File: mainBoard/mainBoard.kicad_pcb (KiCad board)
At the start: 4 copper layers, 221.8 x 118.5 mm, 243 parts, among them J1 1366005, J10 Conn_01x06, J11 Conn_01x07, J12 Conn_01x04, J13 Conn_01x04, J14 1714971, J15 Conn_02x05_Odd_Even, J16 Conn_01x02, J17 Conn_01x05, J18 1714971, J4 4DB-P108-02, J5 4DB-P108-02, J6 4DB-P108-02, J7 Conn_01x02, J8 Conn_01x02, J9 Conn_01x02, K1 Relay_SPDT, Q1 IRLML6244TRPBF, Q2 IRLML6244TRPBF, Q3 IRLML6244TRPBF, Q4 IRLML6244TRPBF, Q5 IRLML6244TRPBF, Q6 IRLML6244TRPBF, Q7 IRLML6244TRPBF, Q8 IRLML6244TRPBF, Q9 IRLML6244TRPBF, SW1 SW_SPST, SW2 SW_SPDT, SW3 SW_Push, SW4 SW_Push, U1 MCP1727T-3302E/SN, U10 DS18B20+, U11 DS18B20+, U12 OPA333AIDCKT, U13 DS18B20+, U14 DS18B20+, U15 DS18B20+, U16 100, U17 100, U18 USBLC6-2SC6, U19 USBLC6-4SC6, U2 AP62250WU, U21 100, U22 USBLC6-4SC6, U23 USBLC6-4SC6, U24 USBLC6-4SC6, U25 USBLC6-4SC6, U3 MCP1727T-3302E/SN, U4 STM32F401RETx, U6 MOC3083S-TA1, U7 MOC3083S-TA1, U8 OPA333AIDCKT, U9 OPA333AIDCKT, Y1 ATS240C-E

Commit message: working on pcb
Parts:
- moved R16 2.00 mm to (174.3, 75.2)
- moved R63 0.94 mm to (231.5, 106.2)
- moved R64 0.90 mm to (231.5, 108.0)
- moved R60 0.50 mm to (231.5, 111.2)
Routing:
- net /Project Architecture/TRIAC/L1_F2_OPTO_TOP: track 107.2 -> 112.8 mm
- net /Project Architecture/TRIAC/L1_TOP: track 76.9 -> 79.6 mm
- net /Project Architecture/TRIAC/L1_OPTO_BOT: track 23.2 -> 25.3 mm
- net LN: track 146.3 -> 144.8 mm
- net /Project Architecture/TRIAC/L1_BOT: track 52.4 -> 53.2 mm
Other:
- outline, holes or cut-outs redrawn

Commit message: final hcanges before review post
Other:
- board text added: "Michael Pate Version 3.1 06/2026"
- board text removed: "Michael Pate Version 3.0 06/2026"

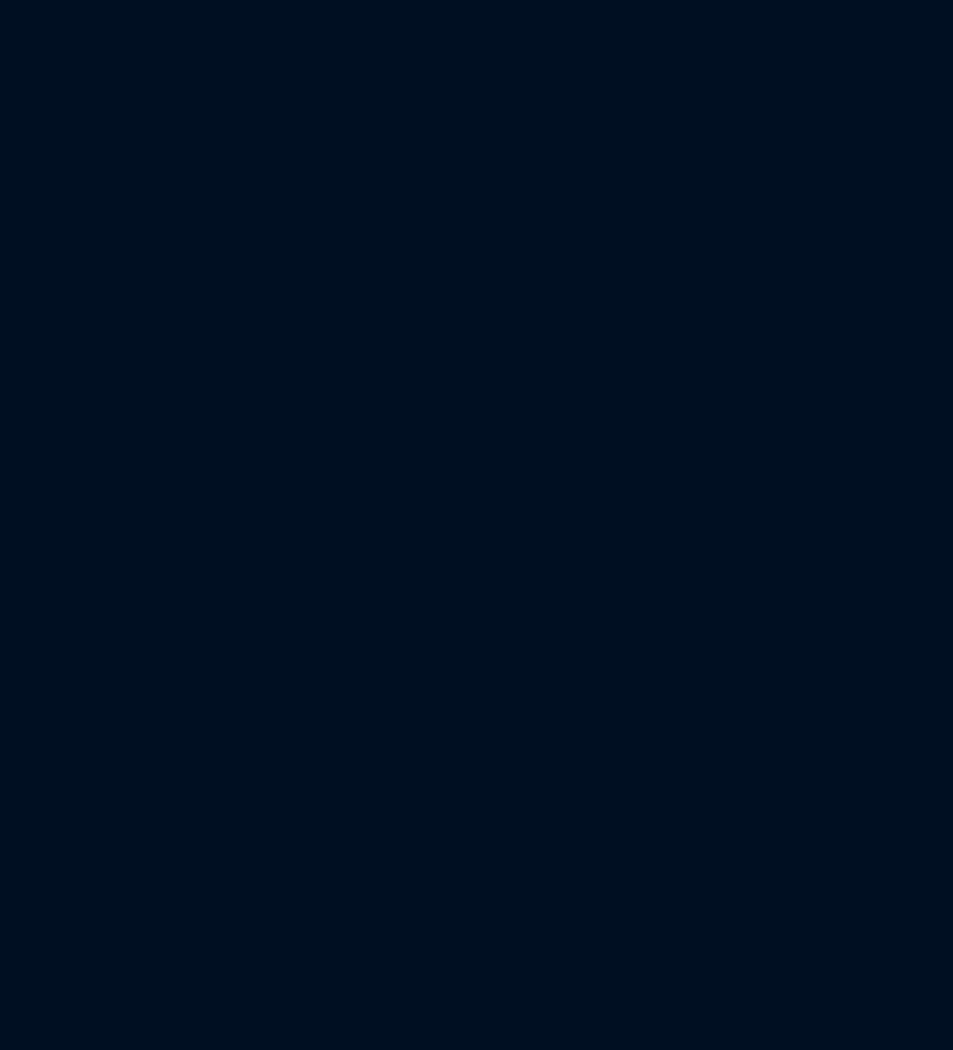
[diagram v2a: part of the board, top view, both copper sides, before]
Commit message: updating power supplies to richtek
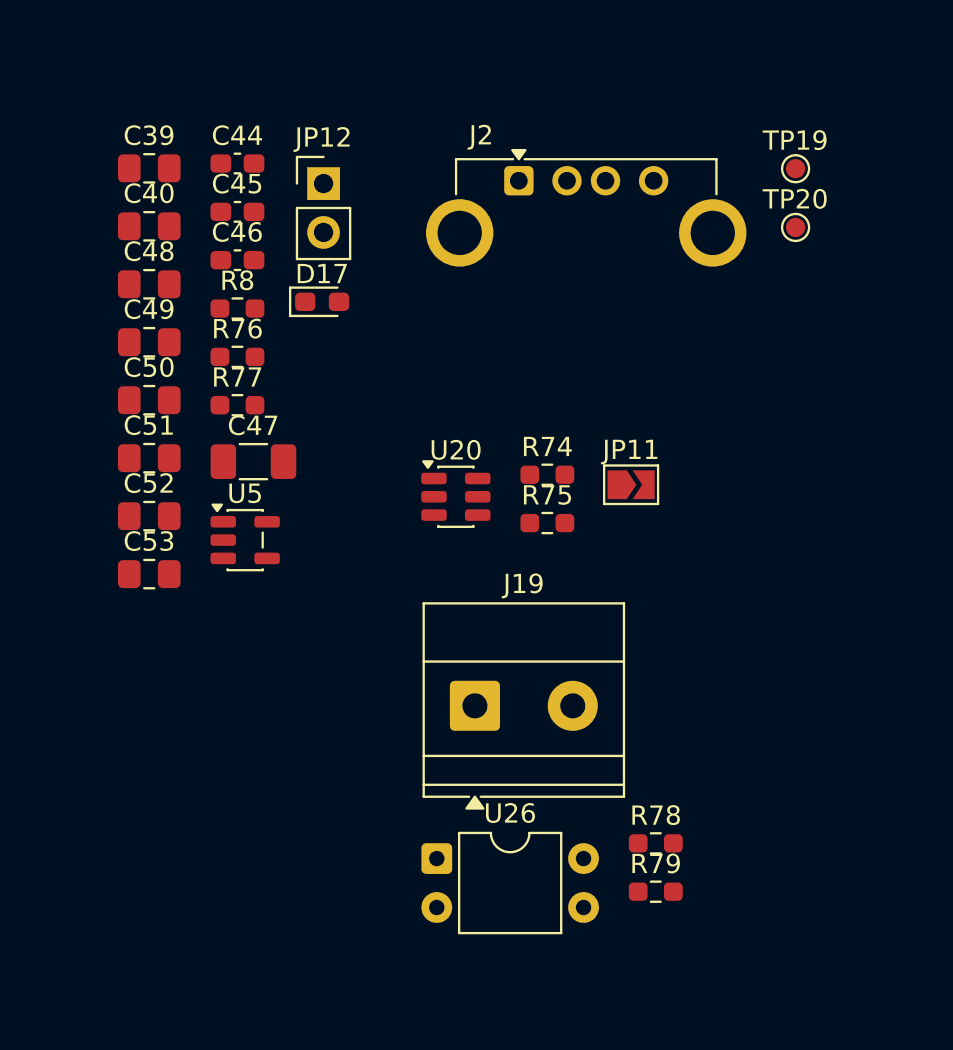
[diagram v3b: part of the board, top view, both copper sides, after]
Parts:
- added C39: 10uF, Capacitor_SMD:C_0805_2012Metric_Pad1.18x1.45mm_HandSolder, F.Cu at (325.3, 106.6)
- added C40: 10uF, Capacitor_SMD:C_0805_2012Metric_Pad1.18x1.45mm_HandSolder, F.Cu at (325.3, 109.6)
- added C44: 100nF, Capacitor_SMD:C_0603_1608Metric_Pad1.08x0.95mm_HandSolder, F.Cu at (329.9, 106.4)
- added C45: 100nF, Capacitor_SMD:C_0603_1608Metric_Pad1.08x0.95mm_HandSolder, F.Cu at (329.9, 108.9)
- added C46: 10uF, Capacitor_SMD:C_0603_1608Metric_Pad1.08x0.95mm_HandSolder, F.Cu at (329.9, 111.4)
- added C47: 10uF, Capacitor_SMD:C_1206_3216Metric_Pad1.33x1.80mm_HandSolder, F.Cu at (330.7, 121.8)
- added C48: 10uF, Capacitor_SMD:C_0805_2012Metric_Pad1.18x1.45mm_HandSolder, F.Cu at (325.3, 112.6)
- added C49: 10uF, Capacitor_SMD:C_0805_2012Metric_Pad1.18x1.45mm_HandSolder, F.Cu at (325.3, 115.6)
- added C50: 10uF, Capacitor_SMD:C_0805_2012Metric_Pad1.18x1.45mm_HandSolder, F.Cu at (325.3, 118.6)
- added C51: 10uF, Capacitor_SMD:C_0805_2012Metric_Pad1.18x1.45mm_HandSolder, F.Cu at (325.3, 121.7)
- added C52: 10uF, Capacitor_SMD:C_0805_2012Metric_Pad1.18x1.45mm_HandSolder, F.Cu at (325.3, 124.7)
- added C53: 10uF, Capacitor_SMD:C_0805_2012Metric_Pad1.18x1.45mm_HandSolder, F.Cu at (325.3, 127.7)
- added D17: RED, LED_SMD:LED_0603_1608Metric_Pad1.05x0.95mm_HandSolder, F.Cu at (334.3, 113.5)
- added J19: Conn_01x02, TerminalBlock_Phoenix:TerminalBlock_Phoenix_MKDS-1,5-2-5.08_1x02_P5.08mm_Horizontal, F.Cu at (342.2, 134.5)
- added J2: USB_A, Connector_USB:USB_A_Connfly_DS1095, F.Cu at (344.5, 107.2)
- added JP11: Jumper_2_Open, Jumper:SolderJumper-2_P1.3mm_Open_TrianglePad1.0x1.5mm, F.Cu at (350.3, 123.0)
- added JP12: Jumper_2_Open, Connector_PinHeader_2.54mm:PinHeader_1x02_P2.54mm_Vertical, F.Cu at (334.4, 107.4)
- added R74: 10k, Resistor_SMD:R_0603_1608Metric_Pad0.98x0.95mm_HandSolder, F.Cu at (346.0, 122.5)
- added R75: 15k, Resistor_SMD:R_0603_1608Metric_Pad0.98x0.95mm_HandSolder, F.Cu at (346.0, 125.0)
- added R76: 10k, Resistor_SMD:R_0603_1608Metric_Pad0.98x0.95mm_HandSolder, F.Cu at (329.9, 116.4)
- added R77: 10k, Resistor_SMD:R_0603_1608Metric_Pad0.98x0.95mm_HandSolder, F.Cu at (329.9, 118.9)
- added R78: 1k, Resistor_SMD:R_0603_1608Metric_Pad0.98x0.95mm_HandSolder, F.Cu at (351.6, 141.7)
- added R79: 1k, Resistor_SMD:R_0603_1608Metric_Pad0.98x0.95mm_HandSolder, F.Cu at (351.6, 144.2)
- added R8: 330, Resistor_SMD:R_0603_1608Metric_Pad0.98x0.95mm_HandSolder, F.Cu at (329.9, 113.9)
- added TP19: TestPoint_Small, TestPoint:TestPoint_Pad_D1.0mm, F.Cu at (358.9, 106.6)
- added TP20: TestPoint_Small, TestPoint:TestPoint_Pad_D1.0mm, F.Cu at (358.9, 109.7)
- added U20: USBLC6-2SC6, Package_TO_SOT_SMD:SOT-23-6, F.Cu at (341.2, 123.7)
- added U26: SFH617A-2, Package_DIP:DIP-4_W7.62mm, F.Cu at (340.2, 142.4)
- added U5: TPS2041B, Package_TO_SOT_SMD:SOT-23-5, F.Cu at (330.3, 125.9)
- C3: value 10uF -> 100uF
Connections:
- C3 pad 1: +12V -> /Project Architecture/Power Supply/+5V_BUCK_VOUT
- U4 pad 10: Net-(U4-PC2) -> Fan2
- U4 pad 11: Net-(U4-PC3) -> Fan3
- U4 pad 2: Net-(U4-PC13) -> ~{DOOR_SW}
- U4 pad 21: Net-(U4-PA5) -> USB_OC
- U4 pad 42: Conv_Fan -> Net-(U4-PA9)
- U4 pad 43: Fan1 -> USB_EN
- U4 pad 44: Fan2 -> USB_DN
- U4 pad 45: Fan3 -> USB_DP
- U4 pad 8: Net-(U4-PC0) -> Conv_Fan
- U4 pad 9: Net-(U4-PC1) -> Fan1
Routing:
- net Net-(U4-PC3): vias 1 -> 0
- net Net-(U4-PC2): vias 1 -> 0
- net Net-(U4-PC1): vias 1 -> 0
- net Net-(U4-PC0): vias 1 -> 0
- net Fan3: vias 0 -> 1
- net Fan2: vias 0 -> 1
- net Fan1: vias 4 -> 5
- net Conv_Fan: vias 4 -> 5

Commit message: change to single 4" touchscreen for UI instead of keypad and buttons
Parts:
- removed the C34 at (213.8, 106.0)
- removed the C38 at (220.2, 108.6)
- removed the C39 at (152.1, 146.5)
- removed the C39 at (325.3, 106.6)
- removed the C40 at (152.0, 149.1)
- removed the C40 at (325.3, 109.6)
- removed the C42 at (146.0, 146.5)
- removed the C44 at (329.9, 106.4)
- removed C46: 10uF, Capacitor_SMD:C_0603_1608Metric_Pad1.08x0.95mm_HandSolder
- removed C47: 10uF, Capacitor_SMD:C_1206_3216Metric_Pad1.33x1.80mm_HandSolder
- removed C48, C49, C50, C51, C52, C53: 10uF, Capacitor_SMD:C_0805_2012Metric_Pad1.18x1.45mm_HandSolder
- removed the C9 at (119.3, 116.8)
- removed D17: RED, LED_SMD:LED_0603_1608Metric_Pad1.05x0.95mm_HandSolder
- removed the D8 at (156.2, 109.0)
- removed the D9 at (172.4, 109.0)
- removed the G*** at (406.4, 33.2)
- removed the J13 at (227.2, 146.2)
- removed J19: Conn_01x02, TerminalBlock_Phoenix:TerminalBlock_Phoenix_MKDS-1,5-2-5.08_1x02_P5.08mm_Horizontal
- removed the J7 at (39.2, 127.8)
- removed the JP10 at (65.6, 120.6)
- removed the JP8 at (253.2, 139.2)
- removed the JP9 at (253.2, 132.5)
- removed NT3, NT4: NetTie_2, NetTie:NetTie-2_SMD_Pad0.5mm
- removed Q8, Q9: IRLML6244TRPBF, Package_TO_SOT_SMD:SOT-23
- removed the R46 at (220.2, 110.3)
- removed the R47 at (40.5, 141.8)
- removed the R48 at (133.8, 127.2)
- removed the R49 at (132.5, 135.2)
- removed the R50 at (209.9, 139.1)
- removed the R51 at (40.5, 143.5)
- removed the R52 at (132.9, 130.0)
- removed the R53 at (129.0, 135.2)
- removed the R54 at (209.0, 142.0)
- removed the R57 at (37.2, 107.8)
- removed the R58 at (188.3, 129.8)
- removed the R59 at (37.8, 104.2)
- removed the R60 at (231.5, 111.2)
- removed the R61 at (224.6, 137.3)
- removed the R62 at (224.6, 132.8)
- removed the R63 at (231.5, 106.2)
- removed the TP17 at (217.9, 125.0)
- removed the TP18 at (217.9, 122.8)
- removed the TP19 at (358.9, 106.6)
- removed the TP19 at (209.2, 122.0)
- removed the TP20 at (358.9, 109.7)
- removed the TP20 at (213.5, 121.2)
- removed the TP21 at (210.5, 120.2)
- removed TP22, TP23, TP24, TP25, TP26, TP27, TP28, TP29, TP30, TP31: TestPoint_Small, TestPoint:TestPoint_Pad_D1.0mm
- removed the U14 at (163.0, 119.8)
- removed the U15 at (179.2, 119.8)
- removed the U16 at (200.5, 137.1)
- added C27: 100nF, Capacitor_SMD:C_0603_1608Metric_Pad1.08x0.95mm_HandSolder, F.Cu at (518.5, 69.4)
- added C28: 100nF, Capacitor_SMD:C_0603_1608Metric_Pad1.08x0.95mm_HandSolder, F.Cu at (518.5, 71.9)
- added C29: 100nF, Capacitor_SMD:C_0603_1608Metric_Pad1.08x0.95mm_HandSolder, F.Cu at (518.5, 74.4)
- added C30: 100nF, Capacitor_SMD:C_0603_1608Metric_Pad1.08x0.95mm_HandSolder, F.Cu at (522.9, 64.4)
- added C31: 100nF, Capacitor_SMD:C_0603_1608Metric_Pad1.08x0.95mm_HandSolder, F.Cu at (522.9, 66.9)
- added C32: 10nF, Capacitor_SMD:C_1812_4532Metric_Pad1.57x3.40mm_HandSolder, F.Cu at (536.0, 29.6)
- added C40: 10uF, Capacitor_SMD:C_0603_1608Metric_Pad1.08x0.95mm_HandSolder, F.Cu at (509.1, 46.0)
- added D4: RED, LED_SMD:LED_0603_1608Metric_Pad1.05x0.95mm_HandSolder, F.Cu at (486.8, 79.3)
- added D6: GRN, LED_SMD:LED_0603_1608Metric_Pad1.05x0.95mm_HandSolder, F.Cu at (531.6, 74.1)
- added D7: RED, LED_SMD:LED_0603_1608Metric_Pad1.05x0.95mm_HandSolder, F.Cu at (531.6, 76.7)
- added H7: MountingHole_Pad, MountingHole:MountingHole_3.2mm_M3_Pad_Via, F.Cu at (455.3, 112.1)
- added H8: MountingHole_Pad, MountingHole:MountingHole_3.2mm_M3_Pad_Via, F.Cu at (455.3, 120.0)
- added J14: Conn_01x06, Connector_PinHeader_2.54mm:PinHeader_1x06_P2.54mm_Vertical, F.Cu at (467.1, 34.5)
- added J16: Conn_01x07, Connector_JST:JST_XH_B7B-XH-A_1x07_P2.50mm_Vertical, F.Cu at (477.7, 29.7)
- added J18: Conn_01x04, Connector_JST:JST_XH_B4B-XH-A_1x04_P2.50mm_Vertical, F.Cu at (490.8, 20.0)
- added JP5: Jumper_2_Open, Connector_PinHeader_2.54mm:PinHeader_1x02_P2.54mm_Vertical, F.Cu at (479.7, 65.4)
- added JP6: Jumper_2_Open, Connector_PinHeader_2.54mm:PinHeader_1x02_P2.54mm_Vertical, F.Cu at (484.3, 65.4)
- added JP7: Jumper_2_Open, Jumper:SolderJumper-2_P1.3mm_Open_TrianglePad1.0x1.5mm, F.Cu at (515.6, 95.5)
- added NT1: NetTie_2, NetTie:NetTie-2_SMD_Pad0.5mm, F.Cu at (517.6, 76.4)
- added NT2: NetTie_2, NetTie:NetTie-2_SMD_Pad0.5mm, F.Cu at (517.6, 77.9)
- added R1: 100k, Resistor_SMD:R_0603_1608Metric_Pad0.98x0.95mm_HandSolder, F.Cu at (465.9, 100.5)
- added R26: 39 1W, Resistor_SMD:R_2512_6332Metric_Pad1.40x3.35mm_HandSolder, F.Cu at (511.5, 16.2)
- added R27: 330 1W, Resistor_SMD:R_2512_6332Metric_Pad1.40x3.35mm_HandSolder, F.Cu at (511.5, 21.1)
- added R28: 330 1W, Resistor_SMD:R_2512_6332Metric_Pad1.40x3.35mm_HandSolder, F.Cu at (511.5, 26.0)
- added R29: 330 1W, Resistor_SMD:R_2512_6332Metric_Pad1.40x3.35mm_HandSolder, F.Cu at (511.5, 30.9)
- added R30: 330 1W, Resistor_SMD:R_2512_6332Metric_Pad1.40x3.35mm_HandSolder, F.Cu at (511.5, 35.8)
- added R31: 220, Resistor_SMD:R_0603_1608Metric_Pad0.98x0.95mm_HandSolder, F.Cu at (518.2, 10.1)
- added R32: 220, Resistor_SMD:R_0603_1608Metric_Pad0.98x0.95mm_HandSolder, F.Cu at (518.2, 12.6)
- added R33: 330, Resistor_SMD:R_0603_1608Metric_Pad0.98x0.95mm_HandSolder, F.Cu at (518.2, 15.1)
- added R34: 10k, Resistor_SMD:R_0603_1608Metric_Pad0.98x0.95mm_HandSolder, F.Cu at (518.2, 17.6)
- added R35: 330, Resistor_SMD:R_0603_1608Metric_Pad0.98x0.95mm_HandSolder, F.Cu at (518.2, 20.1)
- added R36: 10k, Resistor_SMD:R_0603_1608Metric_Pad0.98x0.95mm_HandSolder, F.Cu at (518.2, 22.6)
- added R37: 330, Resistor_SMD:R_0603_1608Metric_Pad0.98x0.95mm_HandSolder, F.Cu at (518.2, 25.1)
- added R40: 4.7k, Resistor_SMD:R_0603_1608Metric_Pad0.98x0.95mm_HandSolder, F.Cu at (518.2, 32.6)
- added R66: 1k, Resistor_SMD:R_0603_1608Metric_Pad0.98x0.95mm_HandSolder, F.Cu at (476.4, 12.6)
- added R67: 1k, Resistor_SMD:R_0603_1608Metric_Pad0.98x0.95mm_HandSolder, F.Cu at (476.4, 15.1)
- added R68: 220, Resistor_SMD:R_0603_1608Metric_Pad0.98x0.95mm_HandSolder, F.Cu at (476.4, 17.6)
- added R80: 4.7k, Resistor_SMD:R_0603_1608Metric_Pad0.98x0.95mm_HandSolder, F.Cu at (485.1, 12.6)
- added R81: 100, Resistor_SMD:R_0603_1608Metric_Pad0.98x0.95mm_HandSolder, F.Cu at (485.1, 15.1)
- added R82: 100, Resistor_SMD:R_0603_1608Metric_Pad0.98x0.95mm_HandSolder, F.Cu at (485.1, 17.6)
- added R83: 10k, Resistor_SMD:R_0603_1608Metric_Pad0.98x0.95mm_HandSolder, F.Cu at (485.1, 20.1)
- added TP10: TestPoint_Small, TestPoint:TestPoint_Pad_D1.0mm, F.Cu at (527.3, 83.8)
- added TP11: TestPoint_Small, TestPoint:TestPoint_Pad_D1.0mm, F.Cu at (527.3, 86.9)
- added TP12: TestPoint_Small, TestPoint:TestPoint_Pad_D1.0mm, F.Cu at (527.3, 89.9)
- added TP13: TestPoint_Small, TestPoint:TestPoint_Pad_D1.0mm, F.Cu at (530.3, 80.8)
- added TP14: TestPoint_Small, TestPoint:TestPoint_Pad_D1.0mm, F.Cu at (530.3, 83.8)
- added TP15: TestPoint_Small, TestPoint:TestPoint_Pad_D1.0mm, F.Cu at (530.3, 86.9)
- added TP5: TestPoint_Small, TestPoint:TestPoint_Pad_D1.0mm, F.Cu at (524.2, 80.8)
- added TP6: TestPoint_Small, TestPoint:TestPoint_Pad_D1.0mm, F.Cu at (524.2, 83.8)
- added TP7: TestPoint_Small, TestPoint:TestPoint_Pad_D1.0mm, F.Cu at (524.2, 86.9)
- added TP8: TestPoint_Small, TestPoint:TestPoint_Pad_D1.0mm, F.Cu at (524.2, 89.9)
- added TP9: TestPoint_Small, TestPoint:TestPoint_Pad_D1.0mm, F.Cu at (527.3, 80.8)
- added U10: DS18B20+, Connector_JST:JST_XH_B3B-XH-A_1x03_P2.50mm_Vertical, F.Cu at (523.8, 38.3)
- added U8: MOC3083S-TA1, Package_DIP:SMDIP-6_W9.53mm, F.Cu at (526.9, 22.6)
- added U9: DS18B20+, Connector_JST:JST_XH_B3B-XH-A_1x03_P2.50mm_Vertical, F.Cu at (523.8, 30.5)
- C1: value 22uF -> 1uF; footprint Capacitor_SMD:C_Elec_6.3x5.8 -> Capacitor_SMD:C_0805_2012Metric_Pad1.18x1.45mm_HandSolder
- C12: value 100nF -> 10uF; footprint Capacitor_SMD:C_0603_1608Metric_Pad1.08x0.95mm_HandSolder -> Capacitor_SMD:C_0805_2012Metric_Pad1.18x1.45mm_HandSolder
- C13: value 22uF -> 47uF
- C15: value 20pF -> 1uF; footprint Capacitor_SMD:C_0402_1005Metric_Pad0.74x0.62mm_HandSolder -> Capacitor_SMD:C_0805_2012Metric_Pad1.18x1.45mm_HandSolder
- C16: value 20pF -> 100nF; footprint Capacitor_SMD:C_0402_1005Metric_Pad0.74x0.62mm_HandSolder -> Capacitor_SMD:C_0603_1608Metric_Pad1.08x0.95mm_HandSolder
- C17, C5: value 100nF -> 22uF; footprint Capacitor_SMD:C_0603_1608Metric_Pad1.08x0.95mm_HandSolder -> Capacitor_SMD:C_0805_2012Metric_Pad1.18x1.45mm_HandSolder
- C18: value 2.2uF -> 100nF; footprint Capacitor_SMD:C_0805_2012Metric_Pad1.18x1.45mm_HandSolder -> Capacitor_SMD:C_0603_1608Metric_Pad1.08x0.95mm_HandSolder
- C19: value 1uF -> 22uF
- C2: value 47nF -> 22uF; footprint Capacitor_SMD:C_0603_1608Metric_Pad1.08x0.95mm_HandSolder -> Capacitor_SMD:C_1206_3216Metric_Pad1.33x1.80mm_HandSolder
- C20: value 100nF -> 10uF
- C22, C23: value 100nF -> 20pF; footprint Capacitor_SMD:C_0603_1608Metric_Pad1.08x0.95mm_HandSolder -> Capacitor_SMD:C_0402_1005Metric_Pad0.74x0.62mm_HandSolder
- C25: value 10nF -> 2.2uF; footprint Capacitor_SMD:C_1812_4532Metric_Pad1.57x3.40mm_HandSolder -> Capacitor_SMD:C_0805_2012Metric_Pad1.18x1.45mm_HandSolder
- C26: value 10nF -> 1uF; footprint Capacitor_SMD:C_1812_4532Metric_Pad1.57x3.40mm_HandSolder -> Capacitor_SMD:C_0805_2012Metric_Pad1.18x1.45mm_HandSolder
- C3: value 100uF -> 10uF; footprint KemetA765:CAPAE830X730N -> Capacitor_SMD:C_0805_2012Metric_Pad1.18x1.45mm_HandSolder
- C33: value 10uF -> 10nF; footprint Capacitor_SMD:C_0603_1608Metric_Pad1.08x0.95mm_HandSolder -> Capacitor_SMD:C_1812_4532Metric_Pad1.57x3.40mm_HandSolder
- C4: value 22uF -> 100nF; footprint Capacitor_SMD:C_Elec_6.3x5.8 -> Capacitor_SMD:C_0603_1608Metric_Pad1.08x0.95mm_HandSolder
- C41: value 47nF -> 10uF C0G
- C45: value 100nF -> 10uF C0G
- C6: value 22uF -> 47pF; footprint Capacitor_SMD:C_Elec_6.3x5.8 -> Capacitor_SMD:C_0603_1608Metric_Pad1.08x0.95mm_HandSolder
- C7: value 47nF -> 22uF; footprint Capacitor_SMD:C_0603_1608Metric_Pad1.08x0.95mm_HandSolder -> Capacitor_SMD:C_0805_2012Metric_Pad1.18x1.45mm_HandSolder
- D10, D11: value 1N5819HW-7-F -> RED; footprint Diode_SMD:D_SOD-123 -> LED_SMD:LED_0603_1608Metric_Pad1.05x0.95mm_HandSolder
- D14, D16: value RED -> 1N5819HW-7-F; footprint LED_SMD:LED_0603_1608Metric_Pad1.05x0.95mm_HandSolder -> Diode_SMD:D_SOD-123
- D5: value GRN -> RED
- H1: value MountingHole_Pad -> MountingHole; footprint MountingHole:MountingHole_2.7mm_Pad_Via -> MountingHole:MountingHole_3.2mm_M3
- H2, H3, H4: value MountingHole_Pad -> MountingHole; footprint MountingHole:MountingHole_2.7mm -> MountingHole:MountingHole_3.2mm_M3
- H5, H6: footprint MountingHole:MountingHole_2.7mm -> MountingHole:MountingHole_3.2mm_M3_Pad_Via
- J10: value Conn_01x06 -> Conn_01x02; footprint Connector_PinHeader_2.54mm:PinHeader_1x06_P2.54mm_Vertical -> Connector_JST:JST_XH_B2B-XH-A_1x02_P2.50mm_Vertical
- J11: value Conn_01x07 -> Conn_02x05_Odd_Even; footprint Connector_JST:JST_XH_B7B-XH-A_1x07_P2.50mm_Vertical -> Connector_IDC:IDC-Header_2x05_P2.54mm_Vertical
- J12: value Conn_01x04 -> Conn_01x02; footprint Connector_JST:JST_XH_B4B-XH-A_1x04_P2.50mm_Vertical -> TerminalBlock_Phoenix:TerminalBlock_Phoenix_MKDS-1,5-2-5.08_1x02_P5.08mm_Horizontal
- J15: value Conn_02x05_Odd_Even -> Conn_01x04; footprint Connector_IDC:IDC-Header_2x05_P2.54mm_Vertical -> Connector_JST:JST_XH_B4B-XH-A_1x04_P2.50mm_Vertical
- JP12, JP3: footprint Connector_PinHeader_2.54mm:PinHeader_1x02_P2.54mm_Vertical -> Jumper:SolderJumper-2_P1.3mm_Open_TrianglePad1.0x1.5mm
- L1: value 2.2uH -> 4.7uH
- R11, R18, R19: value 220 -> 10k
- R12: value 39 1W -> 100k; footprint Resistor_SMD:R_2512_6332Metric_Pad1.40x3.35mm_HandSolder -> Resistor_SMD:R_0603_1608Metric_Pad0.98x0.95mm_HandSolder
- R13: value 39 1W -> 10.5k 1%; footprint Resistor_SMD:R_2512_6332Metric_Pad1.40x3.35mm_HandSolder -> Resistor_SMD:R_0603_1608Metric_Pad0.98x0.95mm_HandSolder
- R14: value 330 1W -> 2k 1%; footprint Resistor_SMD:R_2512_6332Metric_Pad1.40x3.35mm_HandSolder -> Resistor_SMD:R_0603_1608Metric_Pad0.98x0.95mm_HandSolder
- R15: value 330 1W -> 1.2k; footprint Resistor_SMD:R_2512_6332Metric_Pad1.40x3.35mm_HandSolder -> Resistor_SMD:R_0603_1608Metric_Pad0.98x0.95mm_HandSolder
- R16, R17: value 330 1W -> 330; footprint Resistor_SMD:R_2512_6332Metric_Pad1.40x3.35mm_HandSolder -> Resistor_SMD:R_0603_1608Metric_Pad0.98x0.95mm_HandSolder
- R2: value 330 -> 5k
- R20, R21: value 330 -> 10k
- R22: value 10k -> 15k
- R23: value 10k -> 220
- R24: value 330 -> 220
- R25: value 330 -> 39 1W; footprint Resistor_SMD:R_0603_1608Metric_Pad0.98x0.95mm_HandSolder -> Resistor_SMD:R_2512_6332Metric_Pad1.40x3.35mm_HandSolder
- R3: value 52.3k 1% -> 10.5k 1%
- R38: value 1k -> 330
- R39, R79: value 1k -> 4.7k
- R4: value 10k 1% -> 2k 1%
- R5: value 330 -> 147k 1%
- R6: value 330 -> 20k 1%
- R64, R74, R76: value 10k -> 1k
- R65: value 100 -> 1k
- R69, R70: value 4.7k -> 10k
- R7: value 1.2k -> 330
- R73: value 1M -> 1k; footprint Resistor_SMD:R_2512_6332Metric_Pad1.40x3.35mm_HandSolder -> Resistor_SMD:R_0603_1608Metric_Pad0.98x0.95mm_HandSolder
- R75: value 15k -> 1k
- R8: value 330 -> 1M; footprint Resistor_SMD:R_0603_1608Metric_Pad0.98x0.95mm_HandSolder -> Resistor_SMD:R_2512_6332Metric_Pad1.40x3.35mm_HandSolder
- R9: value 10k -> 330
- U1: value MCP1727T-3302E/SN -> RT6255BHGJ8F; footprint Package_SO:SOIC-8_3.9x4.9mm_P1.27mm -> Package_TO_SOT_SMD:TSOT-23-8
- U17: value 100 -> SFH617A-2; footprint Resistor_SMD:R_Array_Convex_4x1206 -> Package_DIP:DIP-4_W7.62mm
- U18, U20: value USBLC6-2SC6 -> USBLC6-4SC6
- U2: value AP62250WU -> RT9059GSP; footprint Package_TO_SOT_SMD:TSOT-23-6_HandSoldering -> Package_SO:SOP-8-1EP_4.57x4.57mm_P1.27mm_EP4.57x4.45mm
- U21: value 100 -> USBLC6-4SC6; footprint Resistor_SMD:R_Array_Convex_4x1206 -> Package_TO_SOT_SMD:SOT-23-6
- U22, U25: value USBLC6-4SC6 -> 100; footprint Package_TO_SOT_SMD:SOT-23-6 -> Resistor_SMD:R_Array_Convex_4x1206
- U24: value USBLC6-4SC6 -> USBLC6-2SC6
- U26: value SFH617A-2 -> 100; footprint Package_DIP:DIP-4_W7.62mm -> Resistor_SMD:R_Array_Convex_4x1206
- U3: value MCP1727T-3302E/SN -> RT9059GSP; footprint Package_SO:SOIC-8_3.9x4.9mm_P1.27mm -> Package_SO:SOP-8-1EP_4.57x4.57mm_P1.27mm_EP4.57x4.45mm
- U4: value STM32F401RETx -> TPS2041B; footprint Package_QFP:LQFP-64_10x10mm_P0.5mm -> Package_TO_SOT_SMD:SOT-23-5
- U5: value TPS2041B -> USBLC6-2SC6; footprint Package_TO_SOT_SMD:SOT-23-5 -> Package_TO_SOT_SMD:SOT-23-6
- U6: value MOC3083S-TA1 -> STM32F401RETx; footprint Package_DIP:SMDIP-6_W9.53mm -> Package_QFP:LQFP-64_10x10mm_P0.5mm
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- renumbered C27 to C34, C28 to C35, C29 to C36, C30 to C37, C31 to C38, C32 to C39, C35 to C42, C36 to C43, C37 to C44, C43 to C9, D6 to D8, D7 to D9, F4 to F2, J16 to J13, J18 to J3, J14 to J4, J4 to J5, J5 to J6, J6 to J7, JP7 to JP10, JP5 to JP8, JP6 to JP9, R26 to R41, R27 to R42, R28 to R43, R29 to R44, R30 to R45, R31 to R46, R32 to R47, R33 to R48, R34 to R49, R35 to R50, R36 to R51, R37 to R52, R66 to R53, R68 to R54, R40 to R57, R41 to R58, R42 to R59, R43 to R60, R44 to R61, R45 to R62, R67 to R63, TP5 to TP16, TP6 to TP17, TP8 to TP18, TP9 to TP19, TP13 to TP20, TP14 to TP21, U8 to U11, U9 to U12, U10 to U13, U11 to U14, U12 to U15, U13 to U16
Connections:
- C10 pad 1: /Project Architecture/Power Supply/+5V_BUCK_VOUT -> Net-(JP2-A)
- C11 pad 1: /Project Architecture/Power Supply/AC_DC_+12V -> Net-(U3-EN)
- C12 pad 1: /Project Architecture/Power Supply/AC_DC_+12V -> Net-(U3-EN)
- C13 pad 1: +3.3VA -> /Project Architecture/Power Supply/AC_DC_+12V
- C14 pad 1: +3.3VA -> +5V
- C15 pad 1: /Project Architecture/MCU/HSE_IN -> /Project Architecture/Power Supply/AC_DC_+12V
- C15 pad 2: /Project Architecture/MCU/HSE_GND -> GND
- C16 pad 1: /Project Architecture/MCU/HSE_OUT -> /Project Architecture/Power Supply/AC_DC_+12V
- C16 pad 2: /Project Architecture/MCU/HSE_GND -> GND
- C17 pad 1: GND -> Net-(JP6-A)
- C17 pad 2: NRST_SW -> GND
- C18 pad 1: /Project Architecture/MCU/STM_VCAP -> VBUS
- C19 pad 1: +3.3V -> Net-(JP6-A)
- C2 pad 1: /Project Architecture/Power Supply/LDO_CD_3v3 -> +12V
- C20 pad 1: +3.3V -> VBUS
- C21 pad 1: +3.3V -> +3.3VA
- C22 pad 1: +3.3V -> /Project Architecture/MCU/HSE_IN
- C22 pad 2: GND -> /Project Architecture/MCU/HSE_GND
- C23 pad 1: +3.3V -> /Project Architecture/MCU/HSE_OUT
- C23 pad 2: GND -> /Project Architecture/MCU/HSE_GND
- C24 pad 1: +3.3V -> GND
- C24 pad 2: GND -> NRST_SW
- C25 pad 1: /Project Architecture/TRIAC/L1_F2_RC_TOP -> /Project Architecture/MCU/STM_VCAP
- C25 pad 2: L1_SW -> GND
- C26 pad 1: /Project Architecture/TRIAC/L1_F3_RC_BOT -> +3.3V
- C26 pad 2: L1_SW -> GND
- C3 pad 1: /Project Architecture/Power Supply/+5V_BUCK_VOUT -> +5V
- C33 pad 1: TC1_ADC -> /Project Architecture/TRIAC/L1_F3_RC_BOT
- C33 pad 2: GND -> L1_SW
- C4 pad 1: +3.3V -> Net-(U1-LX)
- C4 pad 2: GND -> Net-(U1-BOOT)
- C41 pad 1: /Project Architecture/Power Supply/5V_BUCK_EN -> TC2_ADC
- C45 pad 1: VBUS -> TC3_ADC
- C5 pad 1: /Project Architecture/Power Supply/+5V_BUCK_SW -> Net-(JP1-A)
- C5 pad 2: /Project Architecture/Power Supply/+5V_BUCK_BST -> GND
- C6 pad 1: +5V -> Net-(JP2-A)
- C6 pad 2: GND -> Net-(C6-Pad2)
- C7 pad 1: /Project Architecture/Power Supply/LDO_CD_3v3A -> Net-(JP1-A)
- C8 pad 1: /Project Architecture/Power Supply/+5V_BUCK_VOUT -> Net-(JP2-A)
- D1 pad 1: /Project Architecture/Power Supply/3V3_K -> Net-(D1-K)
- D1 pad 2: +5V -> +3.3V
- D10 pad 1: +12V -> /Project Architecture/TRIAC/D4_K
- D10 pad 2: /Project Architecture/Peripherals and Connectors/FAN1_MINUS -> +5V
- D11 pad 1: +12V -> /Project Architecture/TRIAC/D9_K
- D11 pad 2: /Project Architecture/Peripherals and Connectors/FAN2_MINUS -> +5V
- D12 pad 2: /Project Architecture/Peripherals and Connectors/FAN3_MINUS -> /Project Architecture/Peripherals and Connectors/FAN1_MINUS
- D13 pad 2: /Project Architecture/Peripherals and Connectors/CONVFAN_RELAY_MINUS -> /Project Architecture/Peripherals and Connectors/FAN2_MINUS
- D14 pad 1: /Project Architecture/MCU/STM_USR_LED2_K -> +12V
- D14 pad 2: STM_USR_LED2 -> /Project Architecture/Peripherals and Connectors/FAN3_MINUS
- D16 pad 1: /Project Architecture/Power Supply/3VA3_K -> +12V
- D16 pad 2: +5V -> /Project Architecture/Peripherals and Connectors/CONVFAN_RELAY_MINUS
- D2 pad 1: /Project Architecture/Power Supply/5V_K -> Net-(D2-K)
- D5 pad 1: /Project Architecture/MCU/STM_USR_LED1_K -> Net-(D5-K)
- D5 pad 2: /Project Architecture/MCU/STM_USR_LED1 -> VBUS
- J10 pad 1: +5V -> /Project Architecture/Peripherals and Connectors/FAN3_MINUS
- J10 pad 2: +5V -> +12V
- J11 pad 1: /Project Architecture/Peripherals and Connectors/KP_ESD_C0 -> NRST_SW
- J11 pad 2: /Project Architecture/Peripherals and Connectors/KP_ESD_C1 -> SWDCLK
- J11 pad 3: /Project Architecture/Peripherals and Connectors/KP_ESD_C2 -> unconnected-(J11-Pin_3-Pad3)
- J11 pad 4: /Project Architecture/Peripherals and Connectors/KP_ESD_R30 -> SWDIO
- J11 pad 5: /Project Architecture/Peripherals and Connectors/KP_ESD_R1 -> GND
- J11 pad 6: /Project Architecture/Peripherals and Connectors/KP_ESD_R2 -> GND
- J11 pad 7: /Project Architecture/Peripherals and Connectors/KP_ESD_R3 -> /Project Architecture/Peripherals and Connectors/STLink_+3v3
- J12 pad 1: GND -> Net-(J12-Pin_1)
- J12 pad 2: /Project Architecture/Peripherals and Connectors/nRST_ESD -> Net-(J12-Pin_2)
- J15 pad 1: NRST_SW -> GND
- J15 pad 2: SWDCLK -> +5V
- J15 pad 3: unconnected-(J15-Pin_3-Pad3) -> I2C_CLK
- J15 pad 4: SWDIO -> I2C_SDA
- J8 pad 1: /Project Architecture/Peripherals and Connectors/FAN2_MINUS -> +12V
- J8 pad 2: +12V -> /Project Architecture/Peripherals and Connectors/FAN1_MINUS
- J9 pad 1: /Project Architecture/Peripherals and Connectors/FAN3_MINUS -> /Project Architecture/Peripherals and Connectors/FAN2_MINUS
- JP1 pad 1: /Project Architecture/Power Supply/LDO_VOUT_+3v3 -> Net-(JP1-A)
- JP11 pad 1: GND -> +5V
- JP11 pad 2: Net-(J2-Shield) -> /Project Architecture/Peripherals and Connectors/STLink_+5v
- JP12 pad 1: +5V -> +3.3V
- JP12 pad 2: Net-(JP12-B) -> /Project Architecture/Peripherals and Connectors/STLink_+3v3
- JP2 pad 1: /Project Architecture/Power Supply/+5V_BUCK_VOUT -> Net-(JP2-A)
- JP3 pad 1: /Project Architecture/Power Supply/AC_DC_+12V -> GNDPWR
- JP3 pad 2: +12V -> GND
- JP4 pad 1: /Project Architecture/Power Supply/LDO_VOUT_+3v3A -> +5V
- JP4 pad 2: +3.3VA -> Net-(JP4-B)
- L1 pad 1: /Project Architecture/Power Supply/+5V_BUCK_SW -> Net-(U1-LX)
- L1 pad 2: /Project Architecture/Power Supply/+5V_BUCK_VOUT -> Net-(JP2-A)
- R10 pad 1: +3.3V -> USB_EN
- R10 pad 2: NRST_SW -> +5V
- R11 pad 1: /Project Architecture/MCU/STM_USR_LED1_K -> USB_OC
- R11 pad 2: GND -> +5V
- R12 pad 1: /Project Architecture/TRIAC/L1_F2_RC_TOP -> Net-(U3-PGOOD)
- R12 pad 2: /Project Architecture/TRIAC/L1_TOP -> Net-(JP6-A)
- R13 pad 1: /Project Architecture/TRIAC/L1_F3_RC_BOT -> Net-(JP6-A)
- R13 pad 2: /Project Architecture/TRIAC/L1_BOT -> Net-(U3-ADJ)
- R14 pad 1: /Project Architecture/TRIAC/L1_OPTO_TOP -> Net-(U3-ADJ)
- R14 pad 2: /Project Architecture/TRIAC/L1_TOP -> GND
- R15 pad 1: L1_SW -> /Project Architecture/Power Supply/12V_K
- R15 pad 2: /Project Architecture/TRIAC/L1_F2_OPTO_TOP -> GND
- R16 pad 1: /Project Architecture/TRIAC/L1_OPTO_BOT -> Net-(D4-K)
- R16 pad 2: /Project Architecture/TRIAC/L1_BOT -> GND
- R17 pad 1: L1_SW -> Net-(D5-K)
- R17 pad 2: /Project Architecture/TRIAC/L1_F3_OPTO_BOT -> GND
- R18 pad 1: Top_Heater -> /Project Architecture/MCU/BOOT0_SW
- R18 pad 2: /Project Architecture/TRIAC/OPTO_FETG_TOP -> /Project Architecture/MCU/BOOT0
- R19 pad 1: Bottom_Heater -> +3.3V
- R19 pad 2: /Project Architecture/TRIAC/OPTO_FETG_BOT -> NRST_SW
- R2 pad 1: /Project Architecture/Power Supply/3V3_K -> Net-(U1-FB)
- R2 pad 2: Net-(Q8-D) -> Net-(C6-Pad2)
- R20 pad 1: /Project Architecture/TRIAC/OPTO_K_TOP -> +3.3V
- R20 pad 2: /Project Architecture/TRIAC/OPTO_FETD_TOP -> /Project Architecture/MCU/STM_USR_BTN
- R21 pad 1: /Project Architecture/TRIAC/OPTO_K_BOT -> Net-(U6-PA9)
- R21 pad 2: /Project Architecture/TRIAC/OPTO_FETD_BOT -> VBUS
- R22 pad 1: /Project Architecture/TRIAC/OPTO_FETG_TOP -> Net-(U6-PA9)
- R23 pad 1: /Project Architecture/TRIAC/OPTO_FETG_BOT -> /Project Architecture/MCU/STM_USR_LED1_K
- R24 pad 1: /Project Architecture/TRIAC/D4_K -> /Project Architecture/MCU/STM_USR_LED2_K
- R24 pad 2: /Project Architecture/TRIAC/OPTO_FETD_TOP -> GND
- R25 pad 1: /Project Architecture/TRIAC/D9_K -> /Project Architecture/TRIAC/L1_F2_RC_TOP
- R25 pad 2: /Project Architecture/TRIAC/OPTO_FETD_BOT -> /Project Architecture/TRIAC/L1_TOP
- R3 pad 1: /Project Architecture/Power Supply/+5V_BUCK_VOUT -> Net-(JP1-A)
- R3 pad 2: /Project Architecture/Power Supply/+5V_BUCK_FB -> Net-(U2-ADJ)
- R38 pad 1: /Project Architecture/Thermocouple/TC1_ADC_RC -> /Project Architecture/TRIAC/D9_K
- R38 pad 2: TC1_ADC -> /Project Architecture/TRIAC/OPTO_FETD_BOT
- R39 pad 1: /Project Architecture/Thermocouple/TC3_ADC_RC -> +3.3V
- R39 pad 2: TC3_ADC -> TRIAC_TOP_TEMP
- R4 pad 1: /Project Architecture/Power Supply/+5V_BUCK_FB -> Net-(U2-ADJ)
- R5 pad 1: /Project Architecture/Power Supply/3VA3_K -> Net-(JP2-A)
- R5 pad 2: Net-(Q9-D) -> Net-(C6-Pad2)
- R55 pad 1: /Project Architecture/Peripherals and Connectors/BUZZER_MINUS -> /Project Architecture/Thermocouple/TC1_ADC_RC
- R55 pad 2: Net-(Q6-D) -> TC1_ADC
- R56 pad 1: Conv_Fan -> /Project Architecture/Thermocouple/TC2_ADC_RC
- R56 pad 2: /Project Architecture/Peripherals and Connectors/CONVFAN_FET_G -> TC2_ADC
- R6 pad 1: /Project Architecture/Power Supply/5V_K -> Net-(C6-Pad2)
- R64 pad 1: Soft_Power -> /Project Architecture/Thermocouple/TC3_ADC_RC
- R64 pad 2: GND -> TC3_ADC
- R65 pad 1: /Project Architecture/Peripherals and Connectors/ESD_PC6 -> Fan1
- R65 pad 2: PC6 -> /Project Architecture/Peripherals and Connectors/FAN1_FET_G
- R69 pad 1: +3.3V -> /Project Architecture/Peripherals and Connectors/FAN1_FET_G
- R69 pad 2: TRIAC_BOT_TEMP -> GND
- R7 pad 1: /Project Architecture/Power Supply/12V_K -> Net-(D1-K)
- R70 pad 1: +3.3V -> /Project Architecture/Peripherals and Connectors/FAN2_FET_G
- R70 pad 2: TRIAC_TOP_TEMP -> GND
- R71 pad 1: /Project Architecture/Power Supply/LDO_PWRGD_3v3 -> /Project Architecture/Peripherals and Connectors/FAN3_FET_G
- R71 pad 2: +5V -> GND
- R72 pad 1: /Project Architecture/Power Supply/LDO_PWRGD_3v3A -> /Project Architecture/Peripherals and Connectors/BUZ_FET_G
- R72 pad 2: +5V -> GND
- R73 pad 1: LN -> /Project Architecture/Peripherals and Connectors/BUZZER_MINUS
- R73 pad 2: L1_SW -> Net-(Q6-D)
- R74 pad 1: Net-(U4-PA9) -> +3.3V
- R74 pad 2: VBUS -> DOOR_SW
- R75 pad 1: Net-(U4-PA9) -> /Project Architecture/Peripherals and Connectors/D15_K
- R75 pad 2: GND -> /Project Architecture/Peripherals and Connectors/CONVFAN_RELAY_MINUS
- R76 pad 1: USB_OC -> Conv_Fan
- R76 pad 2: +5V -> /Project Architecture/Peripherals and Connectors/CONVFAN_FET_G
- R77 pad 1: USB_EN -> /Project Architecture/Peripherals and Connectors/CONVFAN_FET_G
- R77 pad 2: +5V -> GND
- R78 pad 1: Net-(J19-Pin_2) -> Net-(J12-Pin_2)
- R79 pad 2: ~{DOOR_SW} -> I2C_SDA
- R8 pad 1: Net-(D17-K) -> LN
- R8 pad 2: GND -> L1_SW
- R9 pad 1: /Project Architecture/MCU/BOOT0_SW -> Net-(D2-K)
- R9 pad 2: /Project Architecture/MCU/BOOT0 -> GND
- U1 pad 1: +5V -> Net-(U1-FB)
- U1 pad 2: +5V -> +12V
- U1 pad 3: +5V -> GND
- U1 pad 5: /Project Architecture/Power Supply/LDO_PWRGD_3v3 -> +12V
- U1 pad 6: /Project Architecture/Power Supply/LDO_CD_3v3 -> Net-(U1-LX)
- U1 pad 7: /Project Architecture/Power Supply/LDO_VOUT_+3v3 -> Net-(U1-BOOT)
- U1 pad 8: /Project Architecture/Power Supply/LDO_VOUT_+3v3 -> unconnected-(U1-PGOOD-Pad8)
- U17 pad 1: KP_Col2 -> Net-(J12-Pin_1)
- U17 pad 2: /Project Architecture/Peripherals and Connectors/KP_ESD_C2 -> GND
- U17 pad 3: KP_Col1 -> GND
- U17 pad 4: /Project Architecture/Peripherals and Connectors/KP_ESD_C1 -> DOOR_SW
- U18 pad 1: /Project Architecture/Peripherals and Connectors/SOF_PWR_ESD -> NRST_SW
- U18 pad 3: /Project Architecture/Peripherals and Connectors/nRST_ESD -> SWDCLK
- U18 pad 4: NRST_SW -> SWDIO
- U18 pad 6: /Project Architecture/Peripherals and Connectors/SOF_PWR_TVS -> unconnected-(U18-I/O4-Pad6)
- U19 pad 1: NRST_SW -> /Project Architecture/Peripherals and Connectors/KP_ESD_R30
- U19 pad 3: SWDCLK -> /Project Architecture/Peripherals and Connectors/KP_ESD_R1
- U19 pad 4: SWDIO -> /Project Architecture/Peripherals and Connectors/KP_ESD_R2
- U19 pad 6: unconnected-(U19-I/O4-Pad6) -> /Project Architecture/Peripherals and Connectors/KP_ESD_R3
- U2 pad 1: GND -> Net-(U2-PGOOD)
- U2 pad 2: /Project Architecture/Power Supply/+5V_BUCK_SW -> +5V
- U2 pad 3: +12V -> +5V
- U2 pad 4: /Project Architecture/Power Supply/+5V_BUCK_FB -> +5V
- U2 pad 5: /Project Architecture/Power Supply/5V_BUCK_EN -> (no net)
- U2 pad 6: /Project Architecture/Power Supply/+5V_BUCK_BST -> Net-(JP1-A)
- U20 pad 1: Net-(J2-D+) -> /Project Architecture/Peripherals and Connectors/KP_ESD_C0
- U20 pad 3: Net-(J2-D-) -> /Project Architecture/Peripherals and Connectors/KP_ESD_C1
- U20 pad 4: USB_DN -> /Project Architecture/Peripherals and Connectors/KP_ESD_C2
- U20 pad 5: VBUS -> +3.3V
- U20 pad 6: USB_DP -> unconnected-(U20-I/O4-Pad6)
- U21 pad 1: /Project Architecture/Peripherals and Connectors/ESD_PB12 -> /Project Architecture/Peripherals and Connectors/ESD_PC6
- U21 pad 2: PB12 -> GND
- U21 pad 3: /Project Architecture/Peripherals and Connectors/ESD_PB13 -> unconnected-(U21-I/O2-Pad3)
- U21 pad 4: PB13 -> unconnected-(U21-I/O3-Pad4)
- U21 pad 5: /Project Architecture/Peripherals and Connectors/ESD_PB14 -> +3.3V
- U21 pad 6: PB14 -> unconnected-(U21-I/O4-Pad6)
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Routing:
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- removed copper zone on F.Cu, net +12V
- removed copper zone on F.Cu, net +3.3V
- removed copper zone on In2.Cu, net +3.3V
- removed copper zone on F.Cu, net +3.3VA
- removed copper zone on F.Cu, net +5V
- removed copper zone on F.Cu, net /Project Architecture/Peripherals and Connectors/FAN2_FET_G
- removed copper zone on F.Cu, net /Project Architecture/Peripherals and Connectors/FAN2_MINUS
- removed copper zone on F.Cu, net /Project Architecture/Peripherals and Connectors/FAN3_FET_G
- removed copper zone on F.Cu, net /Project Architecture/Peripherals and Connectors/FAN3_MINUS
- removed copper zone on B.Cu, net /Project Architecture/Peripherals and Connectors/STLink_+3v3
- removed copper zone on F.Cu, net /Project Architecture/Peripherals and Connectors/STLink_+3v3
- removed copper zone on B.Cu, net /Project Architecture/Peripherals and Connectors/STLink_+5v
- removed copper zone on F.Cu, net /Project Architecture/Peripherals and Connectors/STLink_+5v
- removed copper zone on F.Cu, net /Project Architecture/Power Supply/+5V_BUCK_BST
- removed copper zone on F.Cu, net /Project Architecture/Power Supply/+5V_BUCK_SW
- removed copper zone on F.Cu, net /Project Architecture/Power Supply/+5V_BUCK_VOUT
- removed copper zone on F.Cu, net /Project Architecture/Power Supply/AC_DC_+12V
- removed copper zone on F.Cu, net /Project Architecture/Power Supply/L1_F1
- removed copper zone on F.Cu, net /Project Architecture/Power Supply/LDO_PWRGD_3v3A
- removed copper zone on F.Cu, net /Project Architecture/Power Supply/LDO_VOUT_+3v3
- removed copper zone on F.Cu, net /Project Architecture/Power Supply/LDO_VOUT_+3v3A
- removed copper zone on F.Cu, net /Project Architecture/TRIAC/L1_BOT
- removed copper zone on F.Cu, net /Project Architecture/TRIAC/L1_TOP
- removed copper zone on F.Cu, net /Project Architecture/TRIAC/OPTO_FETD_BOT
- removed copper zone on F.Cu, net /Project Architecture/TRIAC/OPTO_FETD_TOP
- removed copper zone on F.Cu, net /Project Architecture/TRIAC/OPTO_FETG_BOT
- removed copper zone on F.Cu, net /Project Architecture/TRIAC/OPTO_FETG_TOP
- removed copper zone on B.Cu, net GND
- removed copper zone on F.Cu, net GND
- removed copper zone on In1.Cu, net GND
- removed copper zone on F.Cu, net L1-120VAC
- removed copper zone on F.Cu, net L1_SW
- removed copper zone on F.Cu, net LN
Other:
- board size 221.8 x 118.5 mm -> 300 x 247.4 mm
- board text removed: "+12V"
- board text removed: "+3v3"
- board text removed: "+3v3A"
- board text removed: "+5V"
- board text removed: "+5v"
- board text removed: "10A Fuse"
- board text removed: "12V Enable"
- board text removed: "12V Fan 2"
- board text removed: "12V Fan 3"
- board text removed: "12V Input"
- board text removed: "1A Fuse"
- board text removed: "20A"
- board text removed: "3A"
- board text removed: "3V3 Enable"
- board text removed: "3V3A Enable"
- board text removed: "3v3"
- board text removed: "3v3A Input"
- board text removed: "5V"
- board text removed: "5V Enable"
- board text removed: "BOOT0"
- board text removed: "Bootloader"
- board text removed: "Bot. Heating Element"
- board text removed: "Bottom"
- board text removed: "Bottom Element"
- board text removed: "Bottom Heating Element"
- board text removed: "Button Header"
- board text removed: "C0 C1 C2 R0 R1 R2 R3"
- board text removed: "COLD"
- board text removed: "COLD Side"
- board text removed: "Convection Fan"
- board text removed: "Data"
- board text removed: "Error"
- board text removed: "FET TC BOT"
- board text removed: "FET TC TOP"
- board text removed: "GND"
- board text removed: "GPIO"
- board text removed: "Ground"
- board text removed: "HOT"
- board text removed: "HOT Side"
- board text removed: "Heatsinks are electrically isolated"
- board text removed: "I2C OLED"
- board text removed: "IN OUT"
- board text removed: "Keypad Matrix"
- board text removed: "L G N"
- board text removed: "Line"
- board text removed: "Mains Input"
- board text removed: "N G L"
- board text removed: "Neutral"
- board text removed: "Normal"
- board text removed: "Oven Fan"
- board text removed: "PB12"
- board text removed: "PB13"
- board text removed: "PB14"
- board text removed: "PB15"
- board text removed: "PC6"
- board text removed: "PWR"
- board text removed: "Power Switch"
- board text removed: "RST"
- board text removed: "Reset"
- board text removed: "SCL"
- board text removed: "SDA"
- board text removed: "STLink Power"
- board text removed: "STLink Programmer"
- board text removed: "Status"
- board text removed: "TRIAC Heatsink Fan 12V"
- board text removed: "Top"
- board text removed: "Top Heating Element"
- board text removed: "User (PA0)"
